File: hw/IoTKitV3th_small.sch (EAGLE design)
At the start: 16 parts

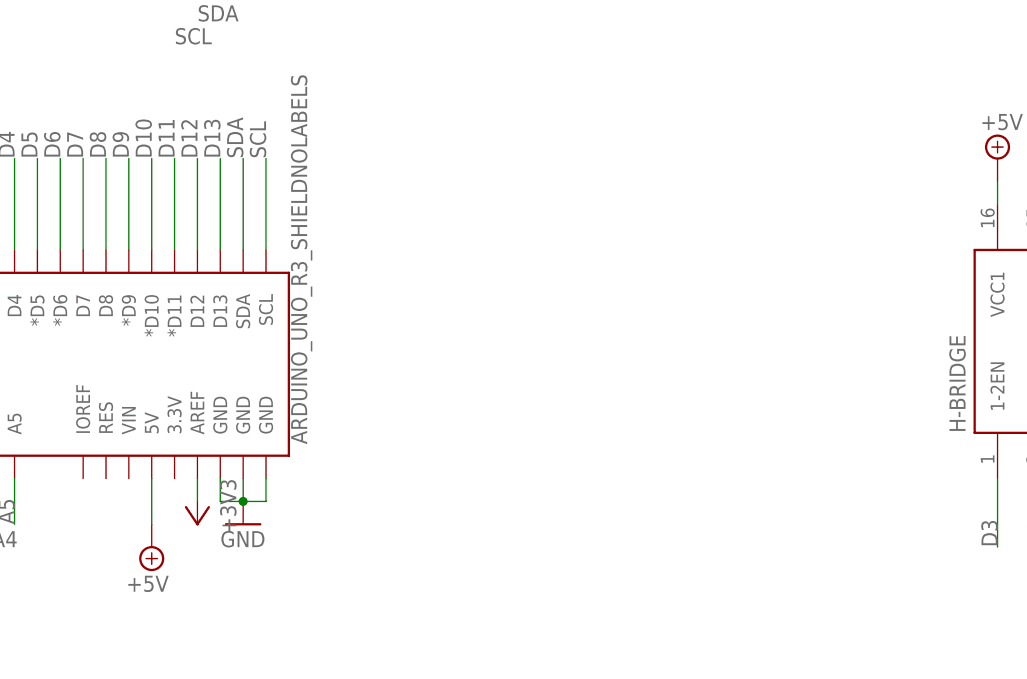
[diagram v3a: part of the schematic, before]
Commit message: V1.2 mit MEMS Temp und Proxi Sensoren
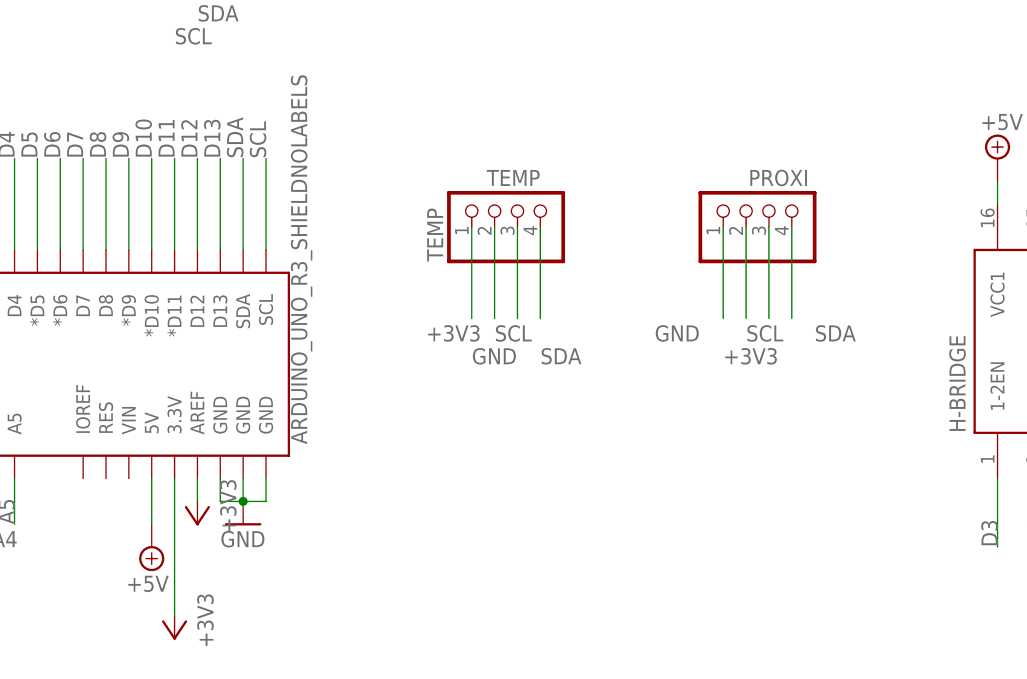
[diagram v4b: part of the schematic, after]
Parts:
- added PROXI: (no value), pinhead:PINHD-1X4
- added TEMP: TEMP, pinhead:PINHD-1X4
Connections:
- net +3V3: now also B1.3.3V, PROXI.2, TEMP.1
- net GND: now also PROXI.1, TEMP.2
- net SCL: now also PROXI.3, TEMP.3
- net SDA: now also PROXI.4, TEMP.4
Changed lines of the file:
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@@
 <part name="SUPPLY1" library="supply2" deviceset="+5V" device=""/>
 <part name="I2C1" library="Seeed-Connector" deviceset="GROVE-CONNECTOR-DIP(4P-2.0)" device="" value="I2C"/>
+<part name="TEMP" library="pinhead" library_urn="urn:adsk.eagle:library:325" deviceset="PINHD-1X4" device="" package3d_urn="urn:adsk.eagle:package:22407/2" value="TEMP"/>
+<part name="PROXI" library="pinhead" library_urn="urn:adsk.eagle:library:325" deviceset="PINHD-1X4" device="" package3d_urn="urn:adsk.eagle:package:22407/2"/>
+<part name="+3V5" library="supply1" library_urn="urn:adsk.eagle:library:371" deviceset="+3V3" device=""/>
 </parts>
 <sheets>
@@
 </instance>
 <instance part="I2C1" gate="G$1" x="40.64" y="93.98" rot="R90"/>
+<instance part="TEMP" gate="A" x="73.66" y="55.88" rot="R90">
+<attribute name="VALUE" x="76.2" y="59.69" size="1.778" layer="96" rot="R180"/>
+</instance>
+<instance part="PROXI" gate="A" x="101.6" y="55.88" rot="R90">
+<attribute name="NAME" x="106.045" y="59.69" size="1.778" layer="95" rot="R180"/>
+<attribute name="VALUE" x="109.22" y="49.53" size="1.778" layer="96" rot="R90"/>
+</instance>
+<instance part="+3V5" gate="G$1" x="35.56" y="7.62" rot="R180">
+<attribute name="VALUE" x="38.1" y="12.7" size="1.778" layer="96" rot="R270"/>
+</instance>
 </instances>
 <busses>
@@
 <label x="38.1" y="76.2" size="1.778" layer="95"/>
 </segment>
+<segment>
+<pinref part="TEMP" gate="A" pin="4"/>
+<wire x1="76.2" y1="53.34" x2="76.2" y2="43.18" width="0.1524" layer="91"/>
+<label x="76.2" y="38.1" size="1.778" layer="95"/>
+</segment>
+<segment>
+<pinref part="PROXI" gate="A" pin="4"/>
+<wire x1="104.14" y1="53.34" x2="104.14" y2="43.18" width="0.1524" layer="91"/>
+<label x="106.68" y="40.64" size="1.778" layer="95"/>
+</segment>
 </net>
 <net name="SCL" class="0">
@@
 <wire x1="36.83" y1="90.17" x2="36.83" y2="83.82" width="0.1524" layer="91"/>
 <label x="35.56" y="73.66" size="1.778" layer="95"/>
+</segment>
+<segment>
+<pinref part="TEMP" gate="A" pin="3"/>
+<wire x1="73.66" y1="53.34" x2="73.66" y2="43.18" width="0.1524" layer="91"/>
+<label x="71.12" y="40.64" size="1.778" layer="95"/>
+</segment>
+<segment>
+<pinref part="PROXI" gate="A" pin="3"/>
+<wire x1="101.6" y1="53.34" x2="101.6" y2="43.18" width="0.1524" layer="91"/>
+<label x="99.06" y="40.64" size="1.778" layer="95"/>
 </segment>
 </net>
@@
 <junction x="88.9" y="96.52"/>
 </segment>
+<segment>
+<pinref part="TEMP" gate="A" pin="2"/>
+<wire x1="71.12" y1="53.34" x2="71.12" y2="43.18" width="0.1524" layer="91"/>
+<label x="68.58" y="38.1" size="1.778" layer="95"/>
+</segment>
+<segment>
+<pinref part="PROXI" gate="A" pin="1"/>
+<wire x1="96.52" y1="53.34" x2="96.52" y2="43.18" width="0.1524" layer="91"/>
+<label x="88.9" y="40.64" size="1.778" layer="95"/>
+</segment>
 </net>
 <net name="+3V3" class="0">
@@
 <wire x1="-20.32" y1="43.18" x2="-20.32" y2="48.26" width="0.1524" layer="91"/>
 </segment>
-</net>
+<segment>
+<pinref part="B1" gate="G$1" pin="3.3V"/>
+<pinref part="+3V5" gate="G$1" pin="+3V3"/>
+<wire x1="35.56" y1="25.4" x2="35.56" y2="10.16" width="0.1524" layer="91"/>
+</segment>
+<segment>
+<pinref part="TEMP" gate="A" pin="1"/>
+<wire x1="68.58" y1="53.34" x2="68.58" y2="43.18" width="0.1524" layer="91"/>
+<label x="63.5" y="40.64" size="1.778" layer="95"/>
+</segment>
+<segment>
+<pinref part="PROXI" gate="A" pin="2"/>
+<wire x1="99.06" y1="53.34" x2="99.06" y2="43.18" width="0.1524" layer="91"/>
+<label x="96.52" y="38.1" size="1.778" layer="95"/>
+</segment>
+</net>

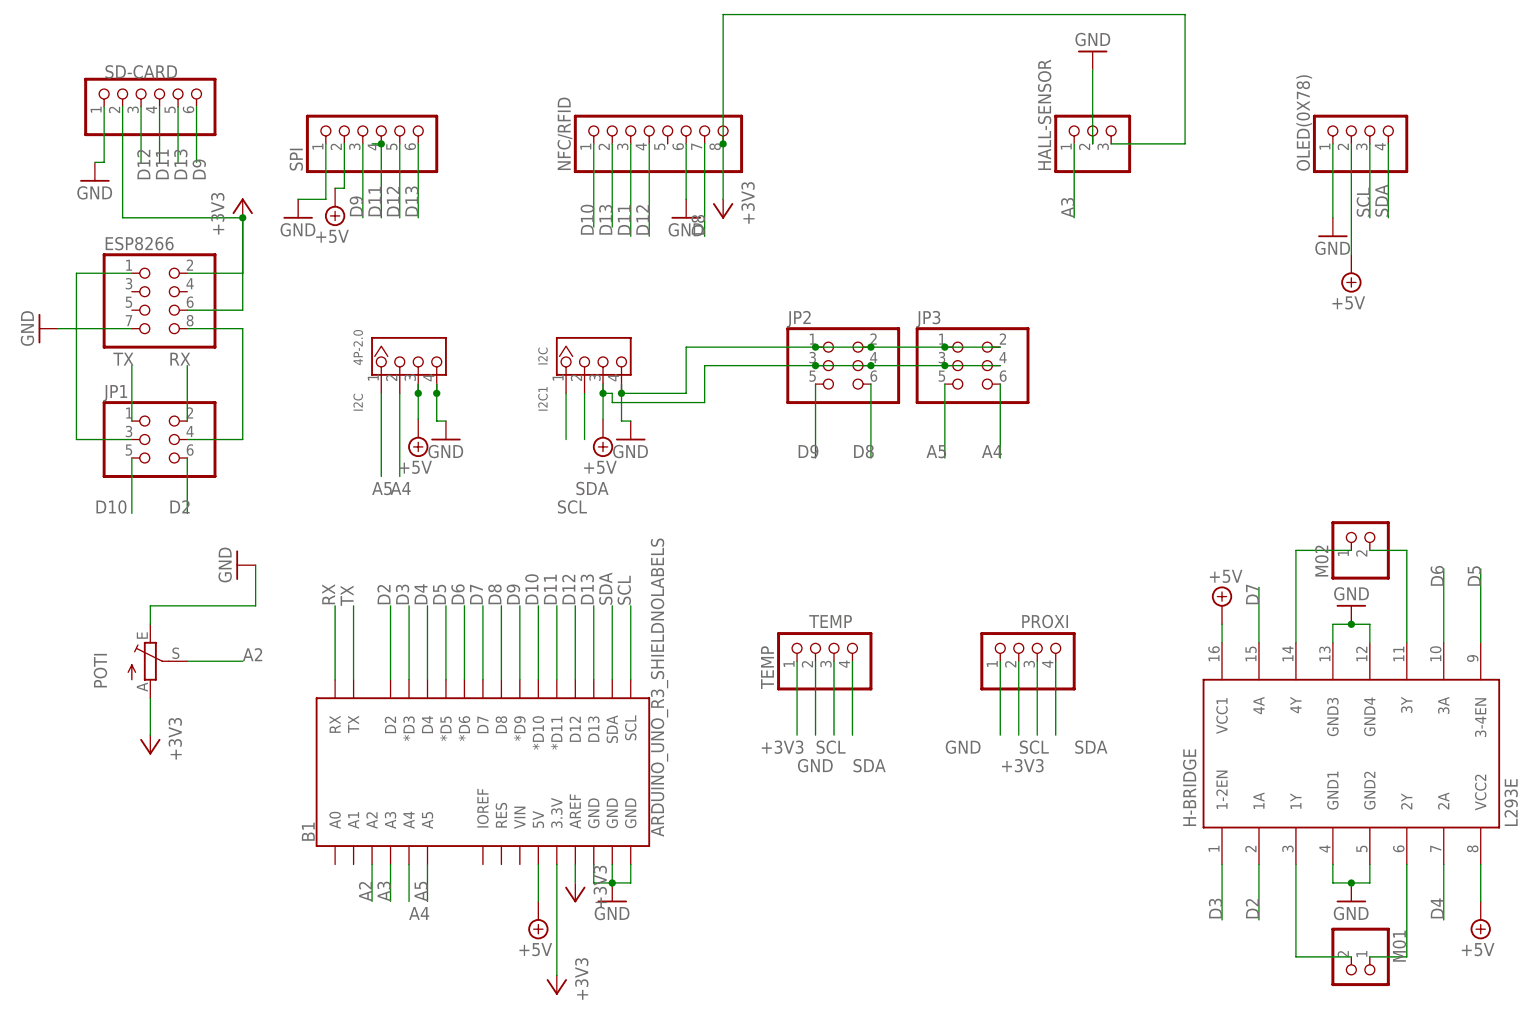
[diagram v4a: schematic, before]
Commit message: Optimierungen SPI, SD Card Adapter, APDS-9960 statt 9930
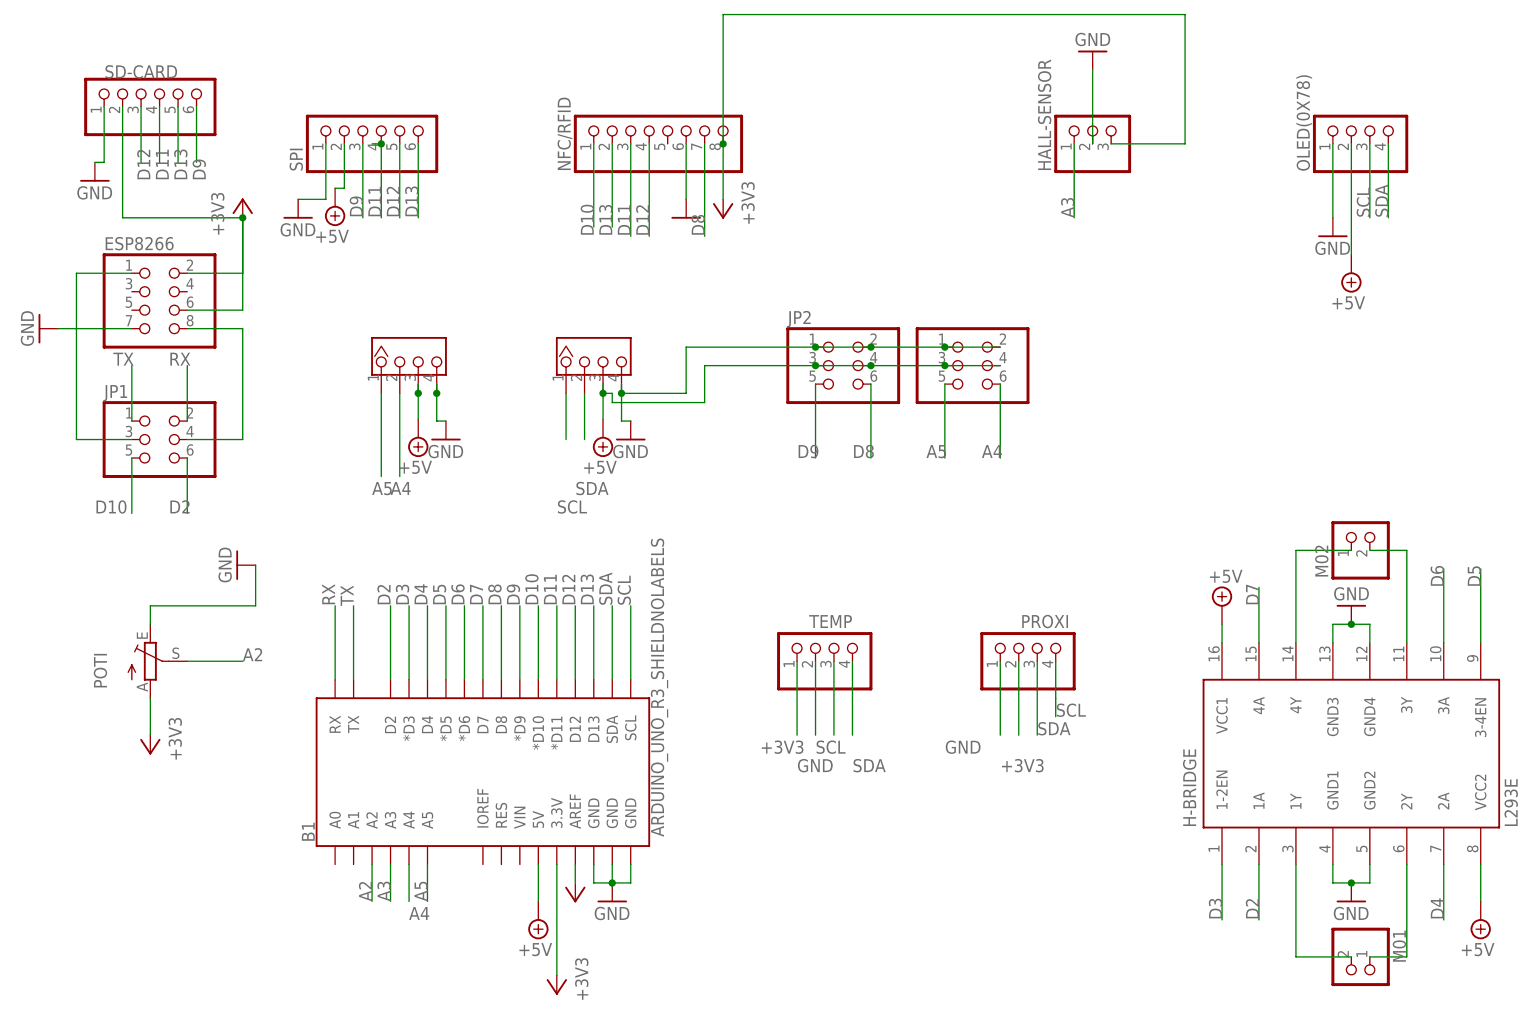
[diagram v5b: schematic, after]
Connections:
- net SCL: now also PROXI.4; no longer PROXI.3
- net SDA: now also PROXI.3; no longer PROXI.4
